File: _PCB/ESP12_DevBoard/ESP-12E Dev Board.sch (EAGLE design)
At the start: 50 parts, among them J1 ZX62-B-5PA(33), J10 DUST, J11 BTN2, J2 I2C, J3 LCD, J4 I2C, J5 LCD_BACKLIGHT, J6 TEMP/HUM, J7 RADON, J8 BTN1, J9 ADC, Q1 UMH3N, U1 5V_REG, U2 3V3_REG, U3 CH340C, U4 TXB0104

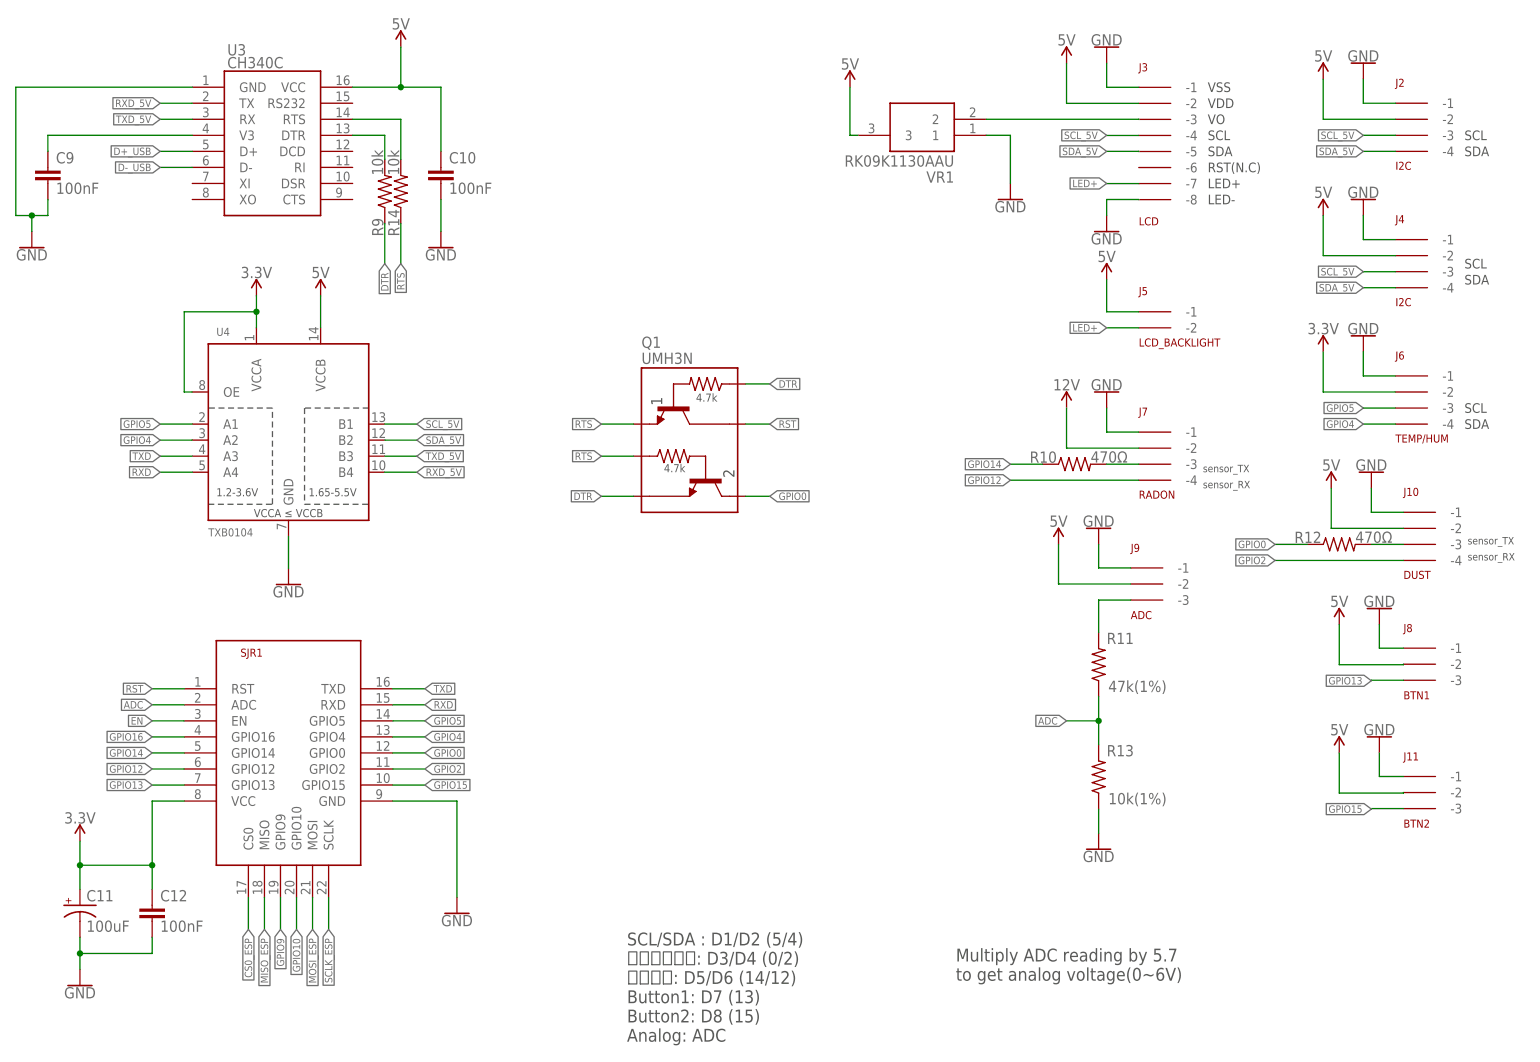
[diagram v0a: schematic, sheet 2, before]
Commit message: PCB edit, broken gerber, BOM to be updated
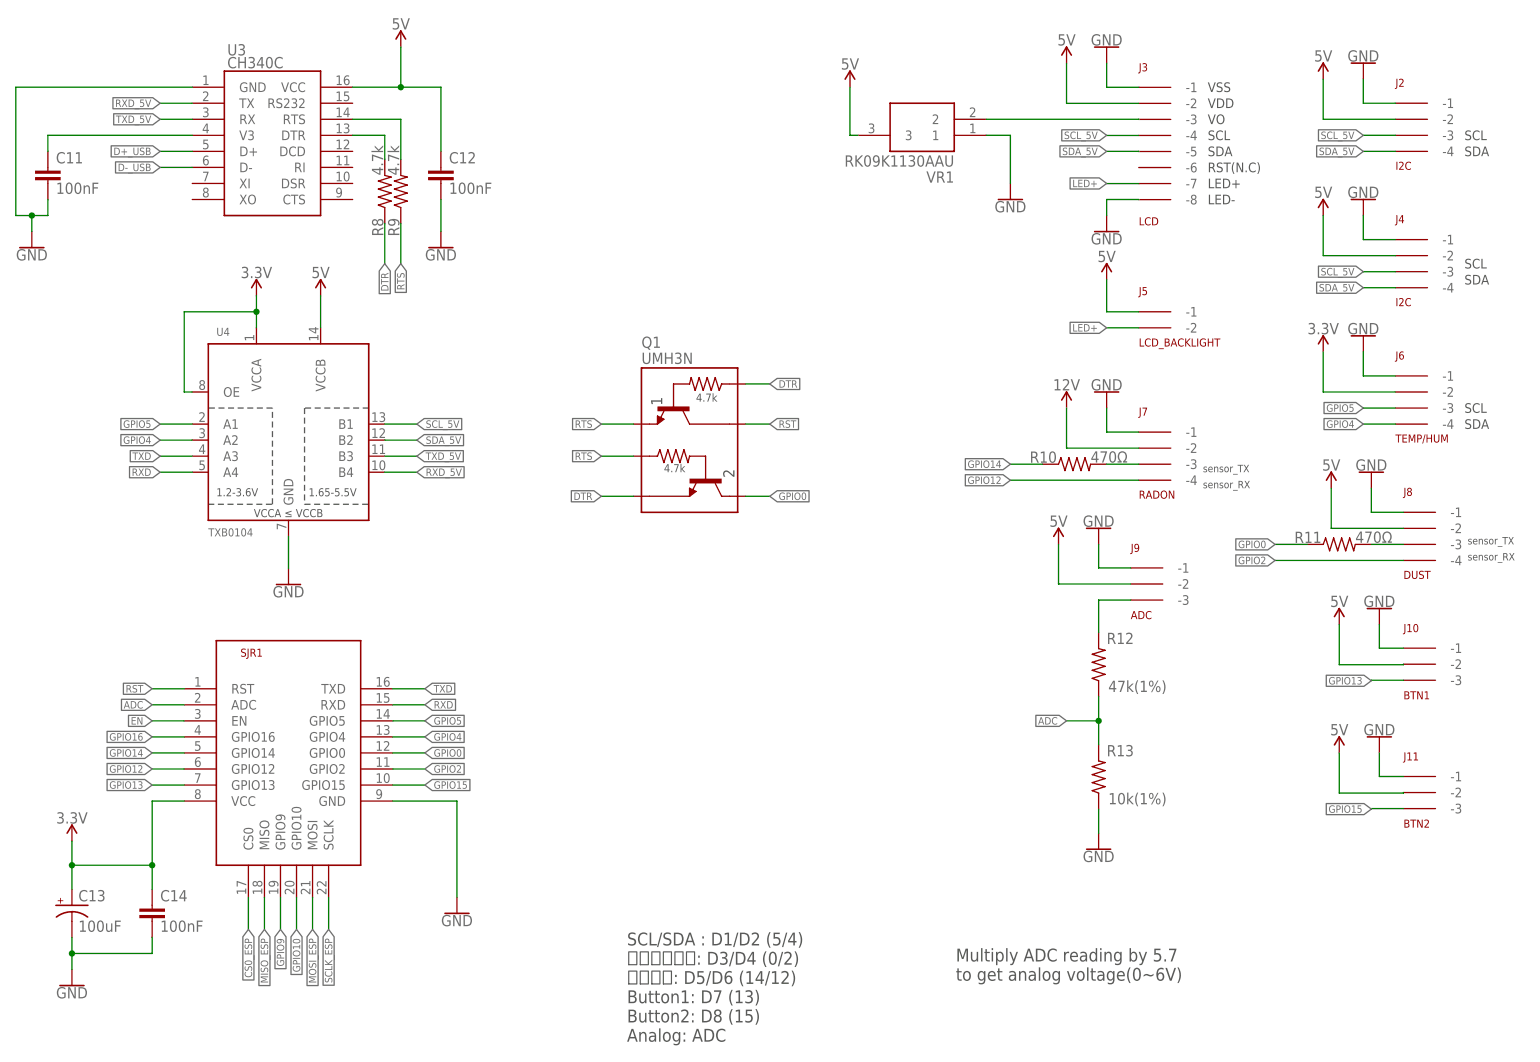
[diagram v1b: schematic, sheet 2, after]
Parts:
- removed R14: 10k, rcl:R-US_R0805
- added C7: 220uF, rcl:CPOL-USUD-6,3X7,7
- added R7: 470Ω, rcl:R-US_R0805
- C10: value 100nF -> 22uF
- C11: value 100uF -> 100nF; device rcl:CPOL-USSMCB -> rcl:C-EUC0805
- C13, C6: value 220uF -> 100uF; device rcl:CPOL-USUD-6,3X7,7 -> rcl:CPOL-USSMCB
- C3: value 10uF -> 100nF
- C4: value 22uF -> 10uF
- C5: value 100uF -> 22uF; device rcl:CPOL-USSMCB -> rcl:C-EUC0805
- C8: value 22uF -> 100nF
- C9: value 100nF -> 220uF; device rcl:C-EUC0805 -> rcl:CPOL-USUD-6,3X7,7
- J10: value DUST -> BTN1; device con-molex-spox:5267-4 -> con-molex-spox:5267-3
- J8: value BTN1 -> DUST; device con-molex-spox:5267-3 -> con-molex-spox:5267-4
- R11: value 47k(1%) -> 470Ω
- R12: value 470Ω -> 47k(1%)
- R8: value 470Ω -> 4.7k
- R9: value 10k -> 4.7k
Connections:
- net 12V: now also C4.1; no longer C3.1
- net 3.3V: now also C10.2, C14.2, C9.+; no longer C11.+, C12.2, C8.2
- net 5V: now also C12.2, C5.1, C7.+; no longer C10.2, C4.1, C5.+
- net ADC: now also R12.1; no longer R11.1
- net DTR: now also R8.1; no longer R9.1
- net EN: now also C3.2
- net GND: now also C11.1, C3.1, C5.2, C7.-, C9.-; no longer C11.-, C3.2, C5.-, C9.1
- net GPIO0: now also R11.1, R7.1; no longer R12.1, R8.1
- net GPIO13: now also J10.-3; no longer J8.-3
- net GPIO2: now also J8.-4; no longer J10.-4
- net N$1: now also C11.2; no longer C9.2
- net N$10: now also C8.2; no longer C14.2
- net N$5: now also R12.2; no longer R11.2
- net N$7: now also R8.2; no longer R9.2
- net N$8: now also R9.2; no longer R14.2
- net N$9: now also J8.-3, R11.2; no longer J10.-3, R12.2
- net POWER1: now also R7.2; no longer R8.2
- net RTS: now also R9.1; no longer R14.1
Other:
- moved on the sheet: C12, C3, C4, C6, C8, R11, R12, R9

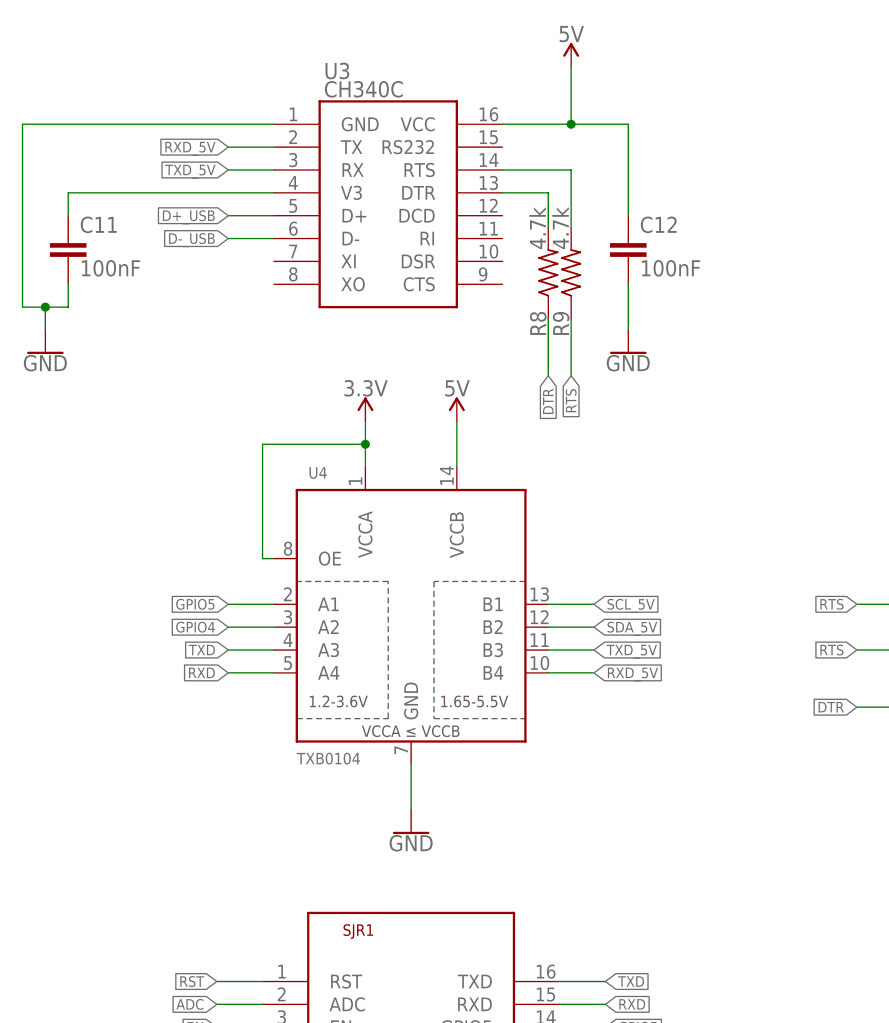
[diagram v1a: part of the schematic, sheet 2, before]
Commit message: ESP-12e dev board PCB 1.4 update
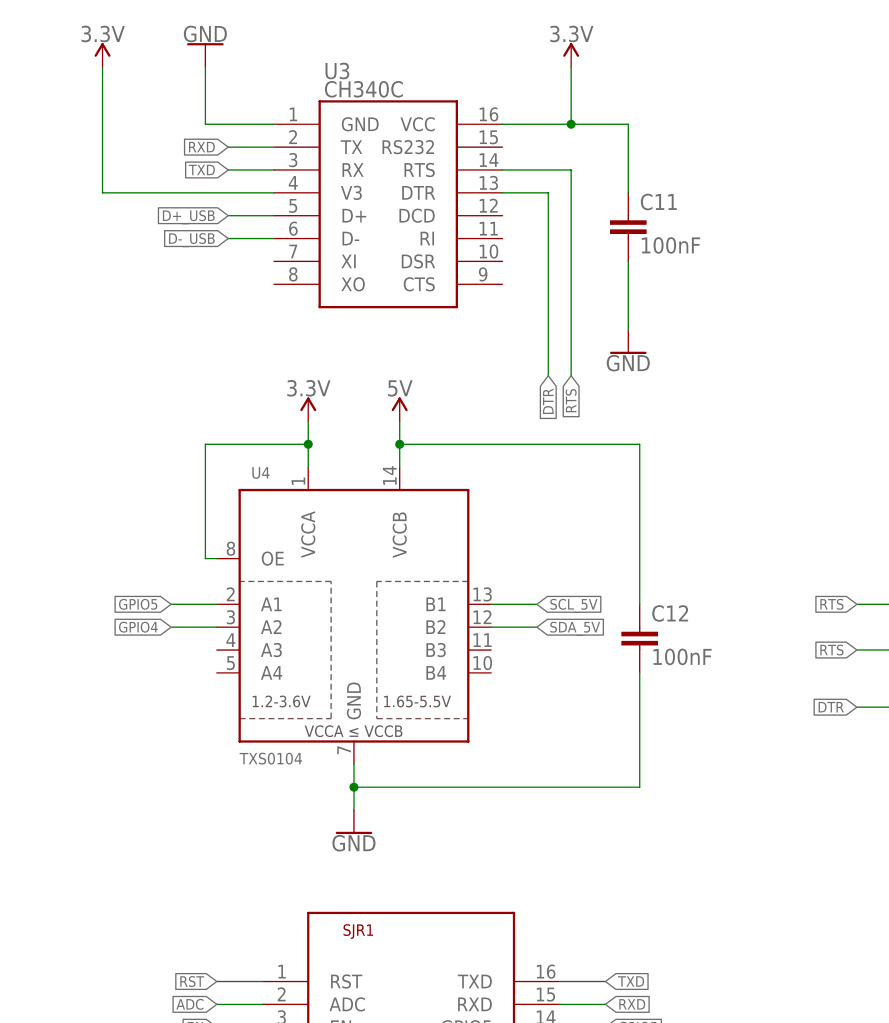
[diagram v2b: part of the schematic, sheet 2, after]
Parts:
- removed R8, R9: 4.7k, rcl:R-US_R0805
- U4: value TXB0104 -> TXS0104
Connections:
- removed net N$1: C11.2, U3.V3
- removed net N$7: R8.2, U3.DTR
- removed net N$8: R9.2, U3.RTS
- removed net RXD_5V: U3.TX, U4.B4
- removed net TXD_5V: U3.RX, U4.B3
- net 3.3V: now also C11.2, U3.V3, U3.VCC
- net 5V: no longer U3.VCC
- net DTR: now also U3.DTR; no longer R8.1
- net RTS: now also U3.RTS; no longer R9.1
- net RXD: now also U3.TX; no longer U4.A4
- net TXD: now also U3.RX; no longer U4.A3
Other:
- moved on the sheet: C11, C12, U4

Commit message: ESP12 dev board V1.4 final commit
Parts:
- removed C14: 100nF, rcl:C-EUC0805
- removed U4: TXS0104, SparkFun-IC-Comms:TXB0104PWR
- C12: value 100nF -> 100uF; device rcl:C-EUC0805 -> rcl:CPOL-USSMCB
- C13: value 100uF -> 100nF; device rcl:CPOL-USSMCB -> rcl:C-EUC0805
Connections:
- removed net SCL_5V: J2.-3, J3.-4, J4.-3, U4.B1
- removed net SDA_5V: J2.-4, J3.-5, J4.-4, U4.B2
- net 3.3V: now also C12.+, C13.2; no longer C13.+, C14.2, U4.OE, U4.VCCA
- net 5V: no longer C12.2, U4.VCCB
- net GND: now also C12.-, C13.1; no longer C12.1, C13.-, C14.1, U4.GND
- net GPIO4: now also J2.-4, J3.-5, J4.-4; no longer U4.A2
- net GPIO5: now also J2.-3, J3.-4, J4.-3; no longer U4.A1
